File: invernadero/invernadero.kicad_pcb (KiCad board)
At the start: 2 copper layers, 114.3 x 101.6 mm, 6 parts, among them J1 Conn_02x20_Odd_Even, J2 Conn_02x20_Odd_Even, J3 Conn_01x08_Pin, J4 Conn_01x16_Socket

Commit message: Diseño de PCB completo
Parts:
- added D1: LED, LED_THT:LED_D4.0mm, F.Cu at (163.8, 82.5)
- added D2: D, Diode_THT:D_DO-41_SOD81_P7.62mm_Horizontal, F.Cu at (160.0, 109.2)
- added G***: LOGO, Custom:pompompurin, B.Cu at (135.9, 101.6)
- added G***: LOGO, Custom:konata2, B.Cu at (113.0, 97.8)
- added J10: Conn_01x02_Socket, TerminalBlock_CUI:TerminalBlock_CUI_TB007-508-02_1x02_P5.08mm_Horizontal, F.Cu at (157.5, 134.6)
- added J5: Conn_01x04_Socket, Connector_PinSocket_2.54mm:PinSocket_1x04_P2.54mm_Vertical, F.Cu at (165.1, 69.8)
- added J6: Conn_01x02_Socket, Connector_PinSocket_2.54mm:PinSocket_1x02_P2.54mm_Vertical, F.Cu at (80.0, 137.2)
- added J7: Conn_01x02_Socket, Connector_PinSocket_2.54mm:PinSocket_1x02_P2.54mm_Vertical, F.Cu at (80.0, 119.4)
- added J8: Conn_01x03_Socket, Connector_PinSocket_2.54mm:PinSocket_1x03_P2.54mm_Vertical, F.Cu at (80.0, 127.0)
- added J9: Conn_01x02_Socket, Connector_PinSocket_2.54mm:PinSocket_1x02_P2.54mm_Vertical, F.Cu at (162.6, 116.8)
- added Q1: NPN, Package_TO_SOT_THT:TO-92_Inline, F.Cu at (162.6, 100.3)
- added R2: 3.3k, Resistor_THT:R_Axial_DIN0204_L3.6mm_D1.6mm_P5.08mm_Horizontal, F.Cu at (142.2, 73.7)
- added R3: 3.3k, Resistor_THT:R_Axial_DIN0204_L3.6mm_D1.6mm_P5.08mm_Horizontal, F.Cu at (147.3, 73.7)
- added R4: 27k, Resistor_THT:R_Axial_DIN0207_L6.3mm_D2.5mm_P7.62mm_Horizontal, F.Cu at (74.9, 121.9)
- added R5: 1.2k, Resistor_THT:R_Axial_DIN0207_L6.3mm_D2.5mm_P7.62mm_Horizontal, F.Cu at (74.9, 139.7)
- added R6: R, Resistor_THT:R_Axial_DIN0204_L3.6mm_D1.6mm_P5.08mm_Horizontal, F.Cu at (161.3, 76.2)
- added R7: R, Resistor_THT:R_Axial_DIN0204_L3.6mm_D1.6mm_P5.08mm_Horizontal, F.Cu at (160.0, 90.2)
- added R8: R, Resistor_THT:R_Axial_DIN0204_L3.6mm_D1.6mm_P5.08mm_Horizontal, F.Cu at (165.1, 94.0)
- R1: footprint Resistor_THT:R_Axial_DIN0207_L6.3mm_D2.5mm_P10.16mm_Horizontal -> Resistor_THT:R_Axial_DIN0204_L3.6mm_D1.6mm_P5.08mm_Horizontal
- moved R1 10.2 mm to (141.0, 139.7), turned to 180 degrees
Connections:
- net Net-(J1-Pin_1) renamed /PC11
- net Net-(J1-Pin_2) renamed /PC10
- net Net-(J1-Pin_3) renamed /PD2
- net Net-(J1-Pin_35) renamed /PC1
- net Net-(J1-Pin_36) renamed /PC2
- net Net-(J1-Pin_37) renamed /PC0
- net Net-(J1-Pin_38) renamed /PC3
- net Net-(J1-Pin_4) renamed /PC12
- J1 pad 15: unconnected-(J1-Pin_15-Pad15) -> +3.3V
- J1 pad 27: unconnected-(J1-Pin_27-Pad27) -> /PA0
- J1 pad 29: unconnected-(J1-Pin_29-Pad29) -> /PA1
- J1 pad 31: unconnected-(J1-Pin_31-Pad31) -> /PA4
- J2 pad 1: unconnected-(J2-Pin_1-Pad1) -> /PC8
- J2 pad 2: unconnected-(J2-Pin_2-Pad2) -> /PC9
- J2 pad 4: unconnected-(J2-Pin_4-Pad4) -> /PB8
- J2 pad 6: unconnected-(J2-Pin_6-Pad6) -> /PB9
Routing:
- net +3.3V: track 0.00 -> 186.5 mm
- net GND: track 21.9 -> 140.2 mm
- net +5V: track 14.3 -> 92.9 mm
- net /PA0: track 0.00 -> 48.3 mm
- net /PA4: track 0.00 -> 37.9 mm
- net /PA1: track 0.00 -> 35.0 mm
- net /PB9: track 0.00 -> 30.1 mm
- net +12V: track 0.00 -> 28.6 mm
- net /PC9: track 0.00 -> 26.4 mm
- net /PB8: track 0.00 -> 21.5 mm
- net Net-(D2-A): track 0.00 -> 19.9 mm
- net Net-(Q1-B): track 0.00 -> 14.1 mm
- net Net-(D1-A): track 0.00 -> 6.35 mm
- net /PC8: track 0.00 -> 6.35 mm
- net Net-(J4-Pin_15): track 3.81 -> 7.18 mm
- added copper zone on B.Cu, net GND
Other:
- board size 114.3 x 101.6 mm -> 100 x 100 mm
- board text added: "Barrenechea Santiago Cafferata Matteo Muñoz Hikary 光 Ovalle Lucas"
- board text added: "Humedad"
- board text added: "Luz"
- board text added: "Temperatura"

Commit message: cambios en el pcb
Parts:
- added R9: 220k, Resistor_THT:R_Axial_DIN0207_L6.3mm_D2.5mm_P7.62mm_Horizontal, F.Cu at (166.4, 108.0)
- J9: footprint Connector_PinSocket_2.54mm:PinSocket_1x02_P2.54mm_Vertical -> TerminalBlock_CUI:TerminalBlock_CUI_TB007-508-02_1x02_P5.08mm_Horizontal
- R6: value R -> 3.3k
- R7, R8: value R -> 1k
- moved D2 37.6 mm to (152.4, 146.1), turned to 90 degrees
- moved J9 20.5 mm to (160.0, 137.2)
- moved Q1 19.1 mm to (161.3, 119.4)
- moved R8 16.9 mm to (161.3, 110.5), turned to -90 degrees
- moved J10 15.5 mm to (160.0, 149.9), turned to 90 degrees
- moved R7 11.5 mm to (161.3, 101.6), turned to -90 degrees
- moved D1 6.35 mm to (160.0, 87.6)
- turned R6 to -90 degrees
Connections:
- R7 pad 2: Net-(Q1-B) -> Net-(R7-Pad2)
- R8 pad 1: Net-(Q1-B) -> Net-(R7-Pad2)
- R8 pad 2: GND -> Net-(Q1-B)
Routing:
- net /PC9: track 26.4 -> 38.5 mm
- net +12V: track 28.6 -> 23.3 mm
- net Net-(D2-A): track 19.9 -> 23.7 mm
- net Net-(R7-Pad2): track 0.00 -> 3.81 mm
- net Net-(Q1-B): track 14.1 -> 11.7 mm
- net Net-(D1-A): track 6.35 -> 6.88 mm
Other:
- board text added: "+ 12V -"
- board text added: "+ FAN -"

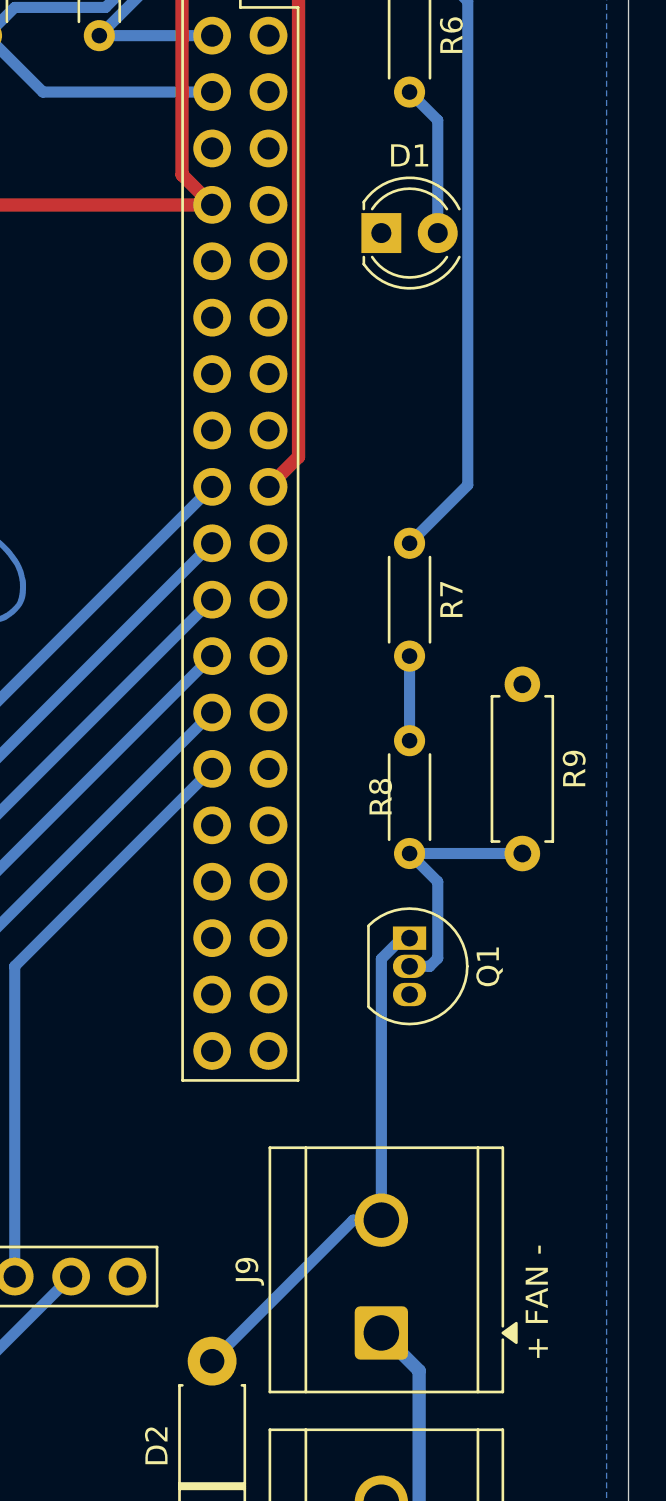
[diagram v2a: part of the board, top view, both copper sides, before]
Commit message: Modificado footprint de led y path de fan más ancho
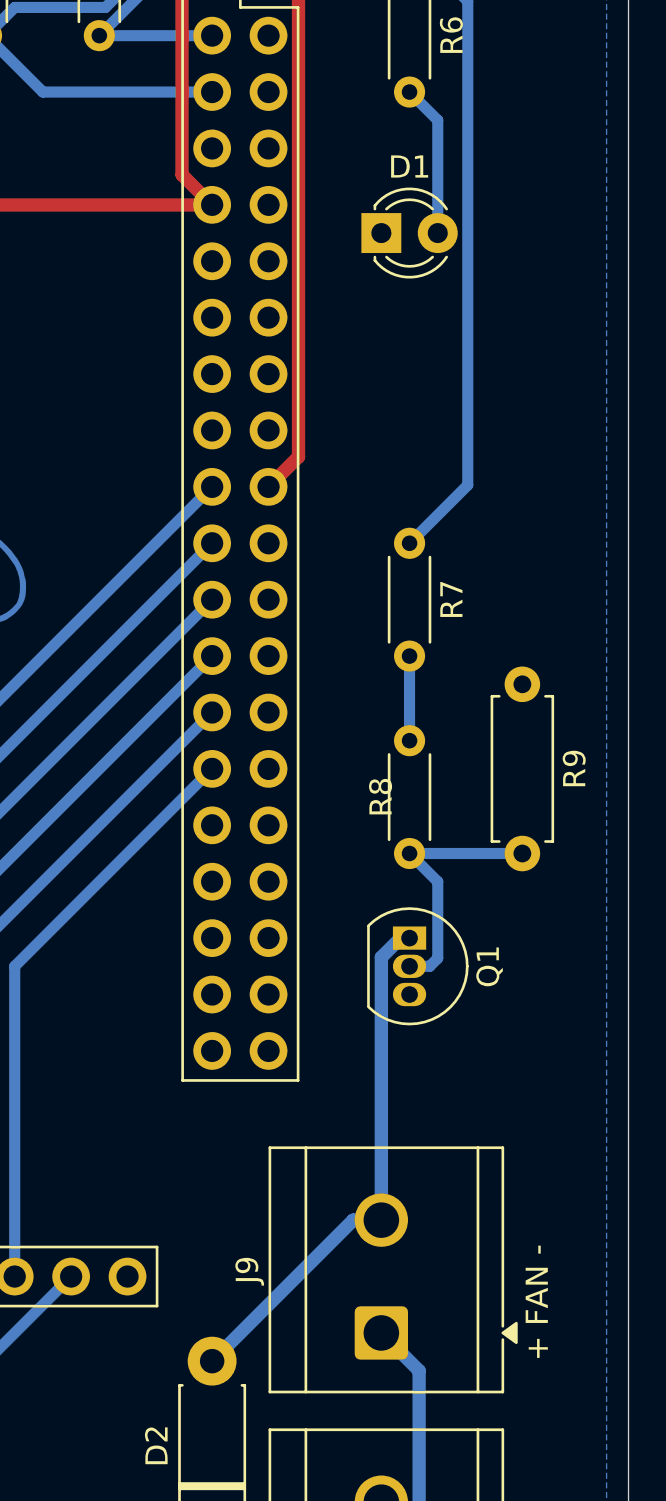
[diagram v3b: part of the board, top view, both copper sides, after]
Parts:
- D1: footprint LED_THT:LED_D4.0mm -> LED_THT:LED_D3.0mm_Clear
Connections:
- net Net-(D2-A) renamed /fan-
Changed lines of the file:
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@@
 	(net 83 "/PC8")
 	(net 84 "Net-(D1-A)")
-	(net 85 "Net-(D2-A)")
+	(net 85 "/fan-")
 	(net 86 "+12V")
 	(net 87 "Net-(Q1-B)")
@@
 		)
 	)
-	(footprint "LED_THT:LED_D4.0mm"
+	(footprint "LED_THT:LED_D3.0mm_Clear"
 		(layer "F.Cu")
 		(at 160.02 87.63)
-		(descr "LED, diameter 4.0mm, 2 pins, https://www.kingbright.com/attachments/file/psearch/000/00/00/L-43GD(Ver.17B).pdf, generated by kicad-footprint-generator")
+		(descr "LED, diameter 3.0mm, 2 pins, clear, generated by kicad-footprint-generator")
 		(tags "LED")
 		(property "Reference" "D1"
-			(at 1.27 -3.46 0)
+			(at 1.27 -2.96 0)
 			(layer "F.SilkS")
 			(effects
@@
 		)
 		(property "Value" "LED"
-			(at 1.27 3.46 0)
+			(at 1.27 2.96 0)
 			(layer "F.Fab")
 			(effects
@@
 		(attr through_hole)
 		(fp_line
-			(start -0.79 -1.399)
-			(end -0.79 -1.08)
+			(start -0.29 -1.236)
+			(end -0.29 -1.08)
 			(stroke
 				(width 0.12)
@@
 		)
 		(fp_line
-			(start -0.79 1.08)
-			(end -0.79 1.399)
+			(start -0.29 1.08)
+			(end -0.29 1.236)
 			(stroke
 				(width 0.12)
@@
 		)
 		(fp_arc
-			(start -0.79 -1.398749)
-			(mid 1.45392 -2.483198)
-			(end 3.513591 -1.08)
+			(start -0.29 -1.235516)
+			(mid 1.36566 -1.987699)
+			(end 2.941437 -1.08)
 			(stroke
 				(width 0.12)
@@
 		)
 		(fp_arc
-			(start -0.41333 -1.08)
-			(mid 1.27 -2)
-			(end 2.95333 -1.08)
+			(start 0.229039 -1.08)
+			(mid 1.27 -1.5)
+			(end 2.310961 -1.08)
 			(stroke
 				(width 0.12)
@@
 		)
 		(fp_arc
-			(start 2.95333 1.08)
-			(mid 1.27 2)
-			(end -0.41333 1.08)
+			(start 2.310961 1.08)
+			(mid 1.27 1.5)
+			(end 0.229039 1.08)
 			(stroke
 				(width 0.12)
@@
 		)
 		(fp_arc
-			(start 3.513591 1.08)
-			(mid 1.45392 2.483198)
-			(end -0.79 1.398749)
+			(start 2.941437 1.08)
+			(mid 1.36566 1.987699)
+			(end -0.29 1.235516)
 			(stroke
 				(width 0.12)
@@
 		)
 		(fp_rect
-			(start -1.44 -2.71)
-			(end 3.98 2.71)
+			(start -1.15 -2.21)
+			(end 3.69 2.21)
 			(stroke
 				(width 0.05)
@@
 		)
 		(fp_line
-			(start -0.73 -1.32665)
-			(end -0.73 1.32665)
+			(start -0.23 -1.16619)
+			(end -0.23 1.16619)
 			(stroke
 				(width 0.1)
@@
 		)
 		(fp_arc
-			(start -0.73 -1.32665)
-			(mid 3.67 0)
-			(end -0.73 1.32665)
+			(start -0.23 -1.16619)
+			(mid 3.17 0)
+			(end -0.23 1.16619)
 			(stroke
 				(width 0.1)
@@
 		(fp_circle
 			(center 1.27 0)
-			(end 3.27 0)
+			(end 2.77 0)
 			(stroke
 				(width 0.1)
@@
 		)
 		(embedded_fonts no)
-		(model "${KICAD9_3DMODEL_DIR}/LED_THT.3dshapes/LED_D4.0mm.step"
+		(model "${KICAD9_3DMODEL_DIR}/LED_THT.3dshapes/LED_D3.0mm_Clear.step"
 			(offset
 				(xyz 0 0 0)
@@
 			(layers "*.Cu" "*.Mask")
 			(remove_unused_layers no)
-			(net 85 "Net-(D2-A)")
+			(net 85 "/fan-")
 			(pinfunction "C")
 			(pintype "open_collector")
@@
 			(layers "*.Cu" "*.Mask")
 			(remove_unused_layers no)
-			(net 85 "Net-(D2-A)")
+			(net 85 "/fan-")
 			(pinfunction "Pin_2")
 			(pintype "passive")
@@
 			(layers "*.Cu" "*.Mask")
 			(remove_unused_layers no)
-			(net 85 "Net-(D2-A)")
+			(net 85 "/fan-")
 			(pinfunction "A")
 			(pintype "passive")
@@
 	)
 	(segment
-		(start 160.02 132.08)
-		(end 160.02 120.314728)
-		(width 0.5)
+		(start 160.02 120.244017)
+		(end 160.02 132.08)
+		(width 0.6)
 		(layer "B.Cu")
 		(net 85)
 	)
 	(segment
-		(start 160.954728 119.38)
-		(end 161.29 119.38)
-		(width 0.5)
+		(start 158.75 132.08)
+		(end 160.02 132.08)
+		(width 0.6)
 		(layer "B.Cu")
 		(net 85)
 	)
 	(segment
-		(start 160.02 120.314728)
-		(end 160.954728 119.38)
-		(width 0.5)
+		(start 152.4 138.43)
+		(end 158.75 132.08)
+		(width 0.6)
 		(layer "B.Cu")
 		(net 85)
 	)
 	(segment
-		(start 158.75 132.08)
-		(end 160.02 132.08)
-		(width 0.5)
+		(start 161.29 119.38)
+		(end 160.884017 119.38)
+		(width 0.6)
 		(layer "B.Cu")
 		(net 85)
 	)
 	(segment
-		(start 152.4 138.43)
-		(end 158.75 132.08)
-		(width 0.5)
+		(start 160.884017 119.38)
+		(end 160.02 120.244017)
+		(width 0.6)
 		(layer "B.Cu")
 		(net 85)

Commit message: Lógica del controlador implementada. Añadido panel de luz. Configuración guarda horas diarias de luz, valor mínimo de luz y temperaturas por día/noche. PCB actualizado.
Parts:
- added D3: LED, LED_THT:LED_D3.0mm_Clear, F.Cu at (158.8, 87.6)
- added R10: 3.3k, Resistor_THT:R_Axial_DIN0204_L3.6mm_D1.6mm_P5.08mm_Horizontal, F.Cu at (161.3, 78.7)
- moved R6 5.68 mm to (166.4, 78.7)
- moved D1 3.81 mm to (163.8, 87.6)
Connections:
- J2 pad 3: unconnected-(J2-Pin_3-Pad3) -> /PC6
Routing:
- net /PC6: track 0.00 -> 6.35 mm
- net /PC8: track 6.35 -> 12.5 mm
- net /PC9: track 38.5 -> 43.1 mm
- net Net-(D3-A): track 0.00 -> 3.81 mm
- net Net-(D1-A): track 6.88 -> 3.81 mm
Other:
- board text added: "Bomba agua"
- board text added: "Panel luz"

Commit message: PCB reordenado. Pistas ensanchadas.
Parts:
- Q1: footprint Package_TO_SOT_THT:TO-92_Inline -> Package_TO_SOT_THT:TO-92_Inline_Wide
- moved J7 27.5 mm to (76.8, 146.7), turned to 90 degrees
- moved J8 21.9 mm to (89.5, 146.7), turned to -90 degrees
- moved R4 20.2 mm to (84.5, 139.7), turned to 90 degrees
- moved J6 18.0 mm to (95.2, 146.7), turned to 90 degrees
- moved R5 17.7 mm to (90.9, 132.1), turned to -90 degrees
- moved J5 3.81 mm to (161.3, 69.8), turned to 180 degrees
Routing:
- net +3.3V: track 186.5 -> 226.3 mm
- net /PA1: track 35.0 -> 42.2 mm
- net /PB9: track 30.1 -> 37.1 mm
- net /PA4: track 37.9 -> 42.6 mm
- net /PB8: track 21.5 -> 24.8 mm
- net +12V: track 23.3 -> 21.2 mm
- net Net-(Q1-B): track 11.7 -> 12.5 mm
- net /PC1: track 38.0 -> 38.7 mm
- net /fan-: track 23.7 -> 24.3 mm
- net /PD2: track 27.2 -> 27.7 mm

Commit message: PCB actualizado
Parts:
- added R11: 560k, Resistor_THT:R_Axial_DIN0204_L3.6mm_D1.6mm_P5.08mm_Horizontal, F.Cu at (85.1, 122.4)
- added R12: 560k, Resistor_THT:R_Axial_DIN0204_L3.6mm_D1.6mm_P5.08mm_Horizontal, F.Cu at (75.7, 122.4)
- added R13: 560k, Resistor_THT:R_Axial_DIN0204_L3.6mm_D1.6mm_P5.08mm_Horizontal, F.Cu at (80.5, 122.4)
- R5: value 1.2k -> 4.7k; footprint Resistor_THT:R_Axial_DIN0207_L6.3mm_D2.5mm_P7.62mm_Horizontal -> Resistor_THT:R_Axial_DIN0204_L3.6mm_D1.6mm_P5.08mm_Horizontal
- moved R4 13.0 mm to (75.7, 130.0), turned to -90 degrees
- moved R5 6.19 mm to (85.1, 130.0)
- moved J8 6.11 mm to (83.8, 144.5), turned to 90 degrees
- moved Q1 5.21 mm to (161.3, 124.6), turned to 90 degrees
- moved RV1 2.92 mm to (100.3, 135.5)
- moved J6 2.63 mm to (93.7, 144.6)
- moved J7 2.19 mm to (76.5, 144.5)
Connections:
- J8 pad 1: /PA1 -> +3.3V
- J8 pad 2: +3.3V -> GND
- J8 pad 3: GND -> /PA1
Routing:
- net /PA1: track 42.2 -> 55.9 mm
- net /PA4: track 42.6 -> 54.7 mm
- net +3.3V: track 226.3 -> 237.5 mm, vias 0 -> 2
- net /PA0: track 48.8 -> 53.4 mm
- net Net-(J4-Pin_3): track 14.0 -> 15.2 mm
- net /fan-: track 24.3 -> 23.4 mm
- net +5V: track 93.1 -> 92.6 mm
